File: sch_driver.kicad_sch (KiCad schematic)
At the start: 31 parts, among them Q1 PSMN4R0-30YLDX, Q2 PSMN4R0-30YLDX, Q3 PSMN4R0-30YLDX, Q4 PSMN4R0-30YLDX, U1 ADA4099-2xR, U10 TMUX1112PWR, U2 ADA4099-2xR

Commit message: WIP - Updating analog switch
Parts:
- removed U10: TMUX1112PWR, $Local:TSSOP-16_4.4x5mm_P0.65mm, symbol $Local:TMUX1112PWR
- added U11, U12, U13, U14, U3: TS5A3159ADCK, $Local:SOT-363_SC-70-6, symbol $Local:TS5A3159ADCK
- renumbered C10 to C3, C9 to C4
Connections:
- net DAC1: now also U11.1, U13.1
- net DAC2: now also U12.1, U14.1
- net GND: now also U11.3, U12.3, U13.3, U14.3
- net REF1: now also U11.4; no longer R21.1
- net REF2: now also U12.4; no longer R22.1
- net REF3: now also U13.4; no longer R23.1
- net REF4: now also U14.4; no longer R24.1
- net SEL1: now also R21.1, U11.6
- net SEL2: now also U12.6
- net SEL3: now also U13.6
- net SEL4: now also U14.6
- no-connect marks 2 -> 0
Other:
- moved on the sheet: C11, C13, C3, C4, Q1, Q3, R1, R11, R13, R21, R23, R3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

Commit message: New analog switch drawn. Updated page borders to B-size sheets.
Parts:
- removed C3, C4: 100nF 50V, $Local:C_0603_1608Metric, symbol $Local:C_0603_100NF_50V
- added C11, C12, C13, C14: 100nF 50V, $Local:C_0603_1608Metric, symbol $Local:C_0603_100NF_50V
- added unit 2 of U12
- added unit 2 of U13
- added unit 2 of U14
- renumbered U3 to U11
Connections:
- net +3.3V: now also U11.5 (V+), C11.1, C12.1, C13.1, C14.1, U12.5 (V+), U13.5 (V+), U14.5 (V+)
- net GND: now also U11.2 (GND), C11.2, C12.2, C13.2, C14.2, U12.2 (GND), U13.2 (GND), U14.2 (GND)
- net SEL2: now also R22.1
- net SEL3: now also R23.1
- net SEL4: now also R24.1
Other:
- moved on the sheet: C1, C11, C12, C13, C14, C2, Q1, Q2, Q3, Q4, R1, R11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

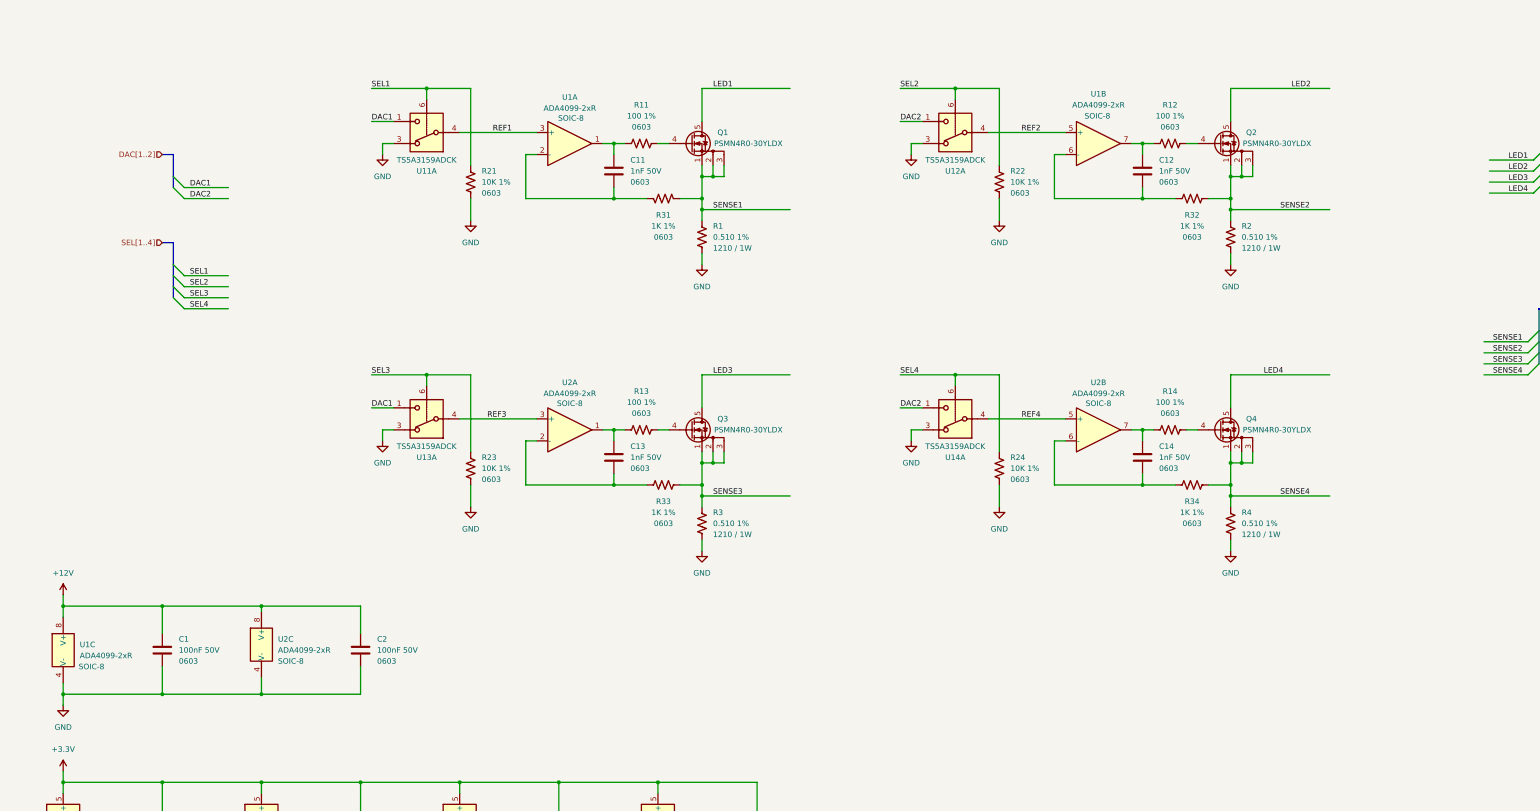
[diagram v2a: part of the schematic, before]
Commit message: Added buffers to current sense signals
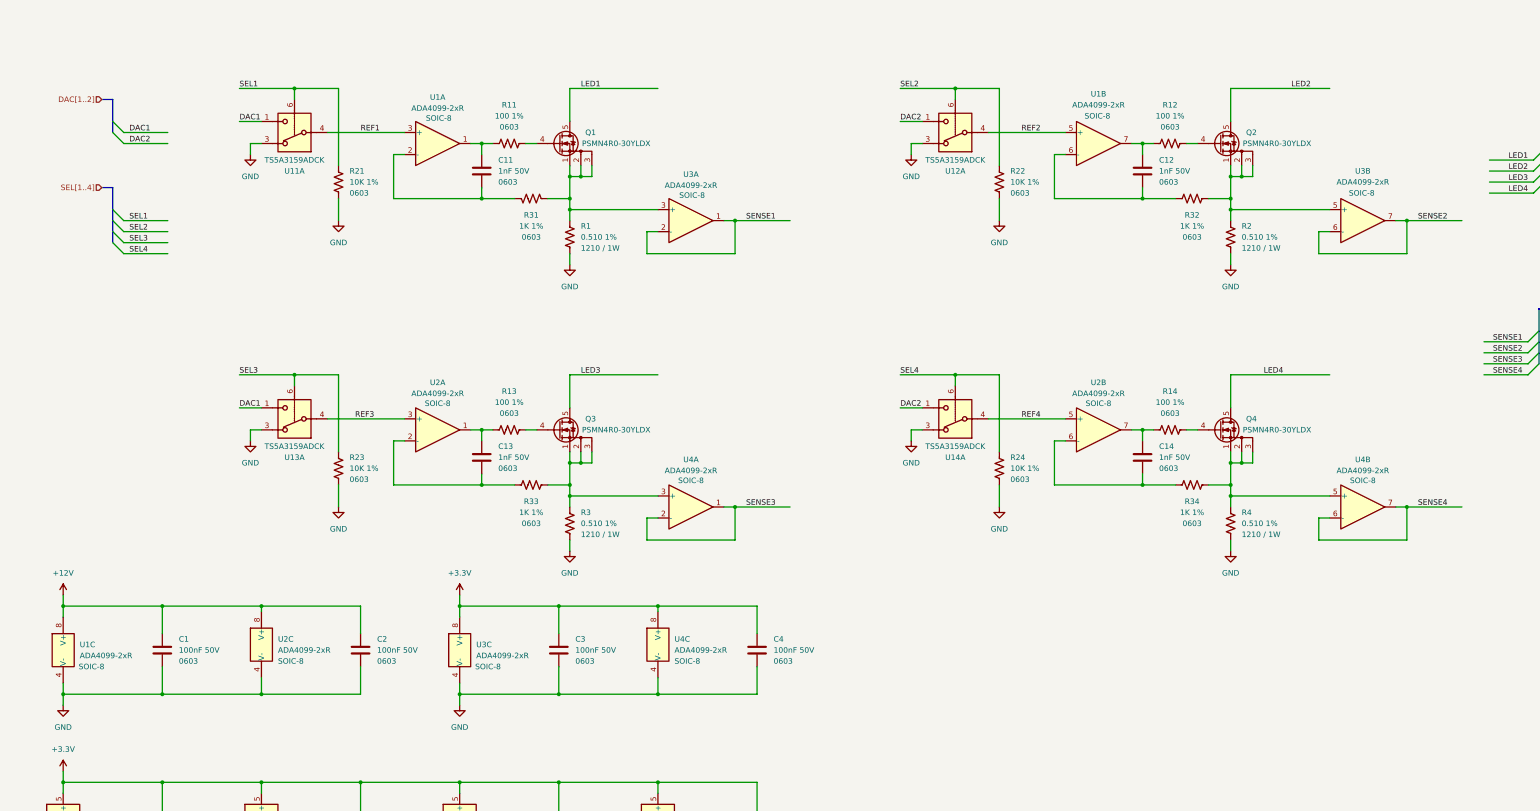
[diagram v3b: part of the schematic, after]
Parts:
- added C3, C4: 100nF 50V, $Local:C_0603_1608Metric, symbol $Local:C_0603_100NF_50V
- added U3, U4: ADA4099-2xR, $Local:SOIC-8_3.9x4.9mm_P1.27mm, symbol $Local:ADA4099-2xR
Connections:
- net +3.3V: now also C3.1, C4.1, U3.8 (V+), U4.8 (V+)
- net GND: now also C3.2, C4.2, U3.4 (V-), U4.4 (V-)
- net SENSE1: now also U3.1, U3.2 (-); no longer Q1.1 (S), Q1.2 (S), Q1.3 (S), R1.1, R31.2
- net SENSE2: now also U3.6 (-), U3.7; no longer Q2.1 (S), Q2.2 (S), Q2.3 (S), R2.1, R32.2
- net SENSE3: now also U4.1, U4.2 (-); no longer Q3.1 (S), Q3.2 (S), Q3.3 (S), R3.1, R33.2
- net SENSE4: now also U4.6 (-), U4.7; no longer Q4.1 (S), Q4.2 (S), Q4.3 (S), R34.2, R4.1
- new net: Q4.1 (S), Q4.2 (S), Q4.3 (S), R34.2, R4.1, U4.5 (+)
- new net: Q3.1 (S), Q3.2 (S), Q3.3 (S), R3.1, R33.2, U4.3 (+)
- new net: Q2.1 (S), Q2.2 (S), Q2.3 (S), R2.1, R32.2, U3.5 (+)
- new net: Q1.1 (S), Q1.2 (S), Q1.3 (S), R1.1, R31.2, U3.3 (+)
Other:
- moved on the sheet: C11, C13, Q1, Q3, R1, R11, R13, R21, R23, R3, R31, R33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

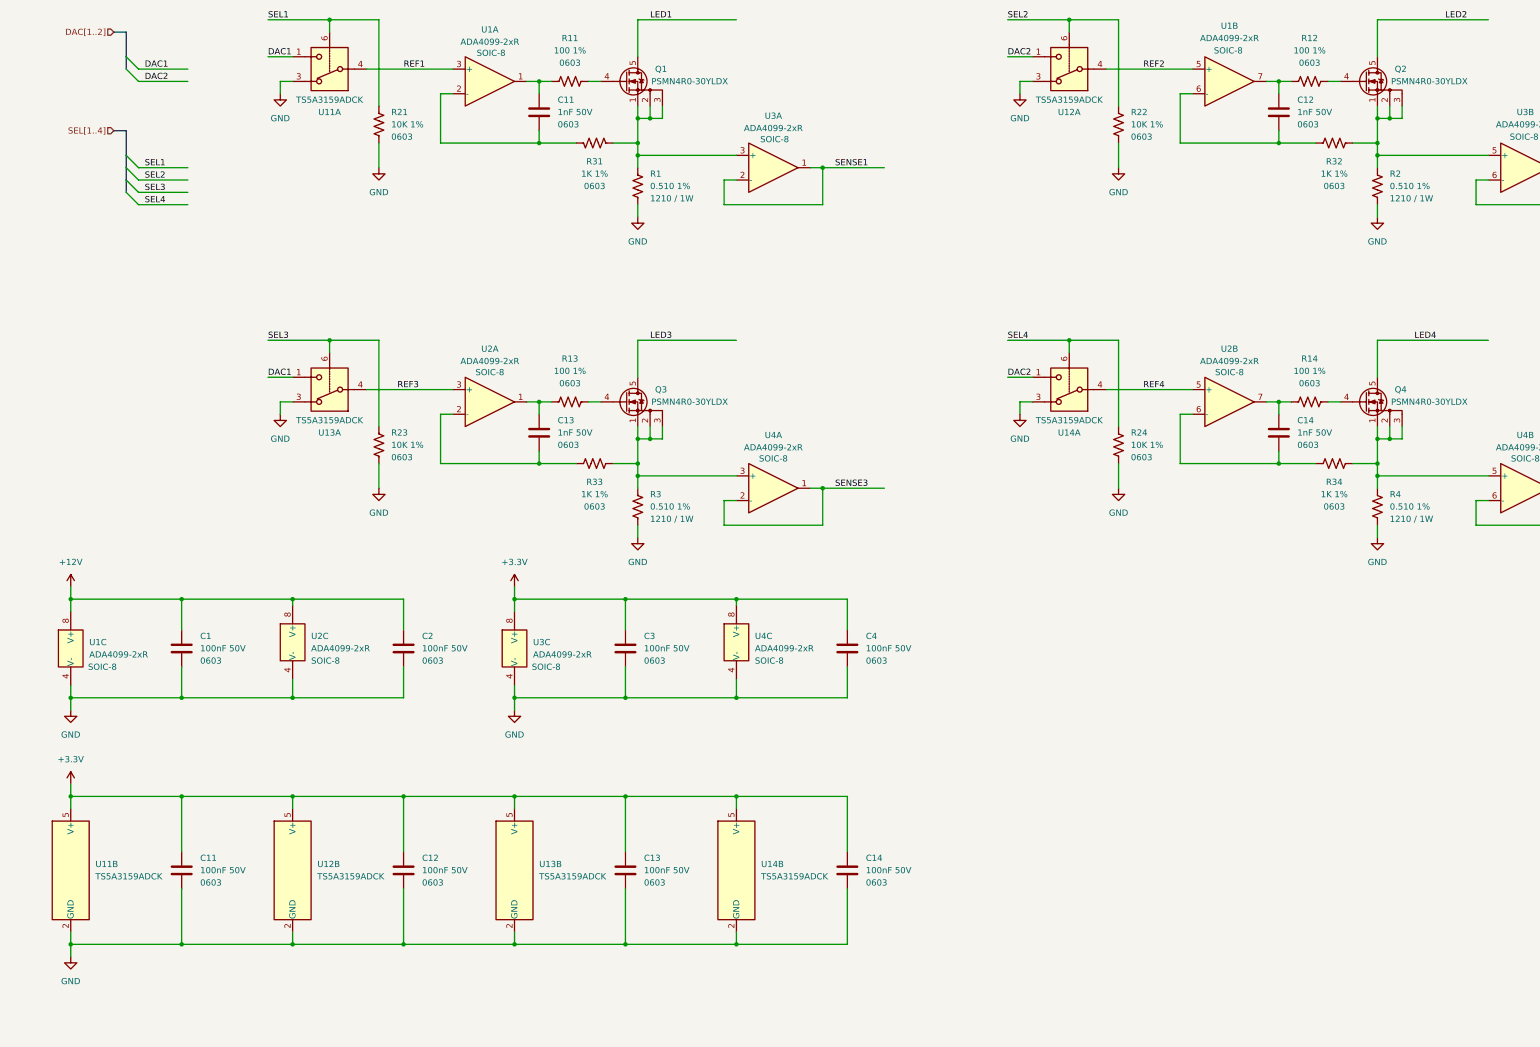
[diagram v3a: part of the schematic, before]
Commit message: Updated 'Size' property to 'Package' on R & C. Cleaned up switch page.
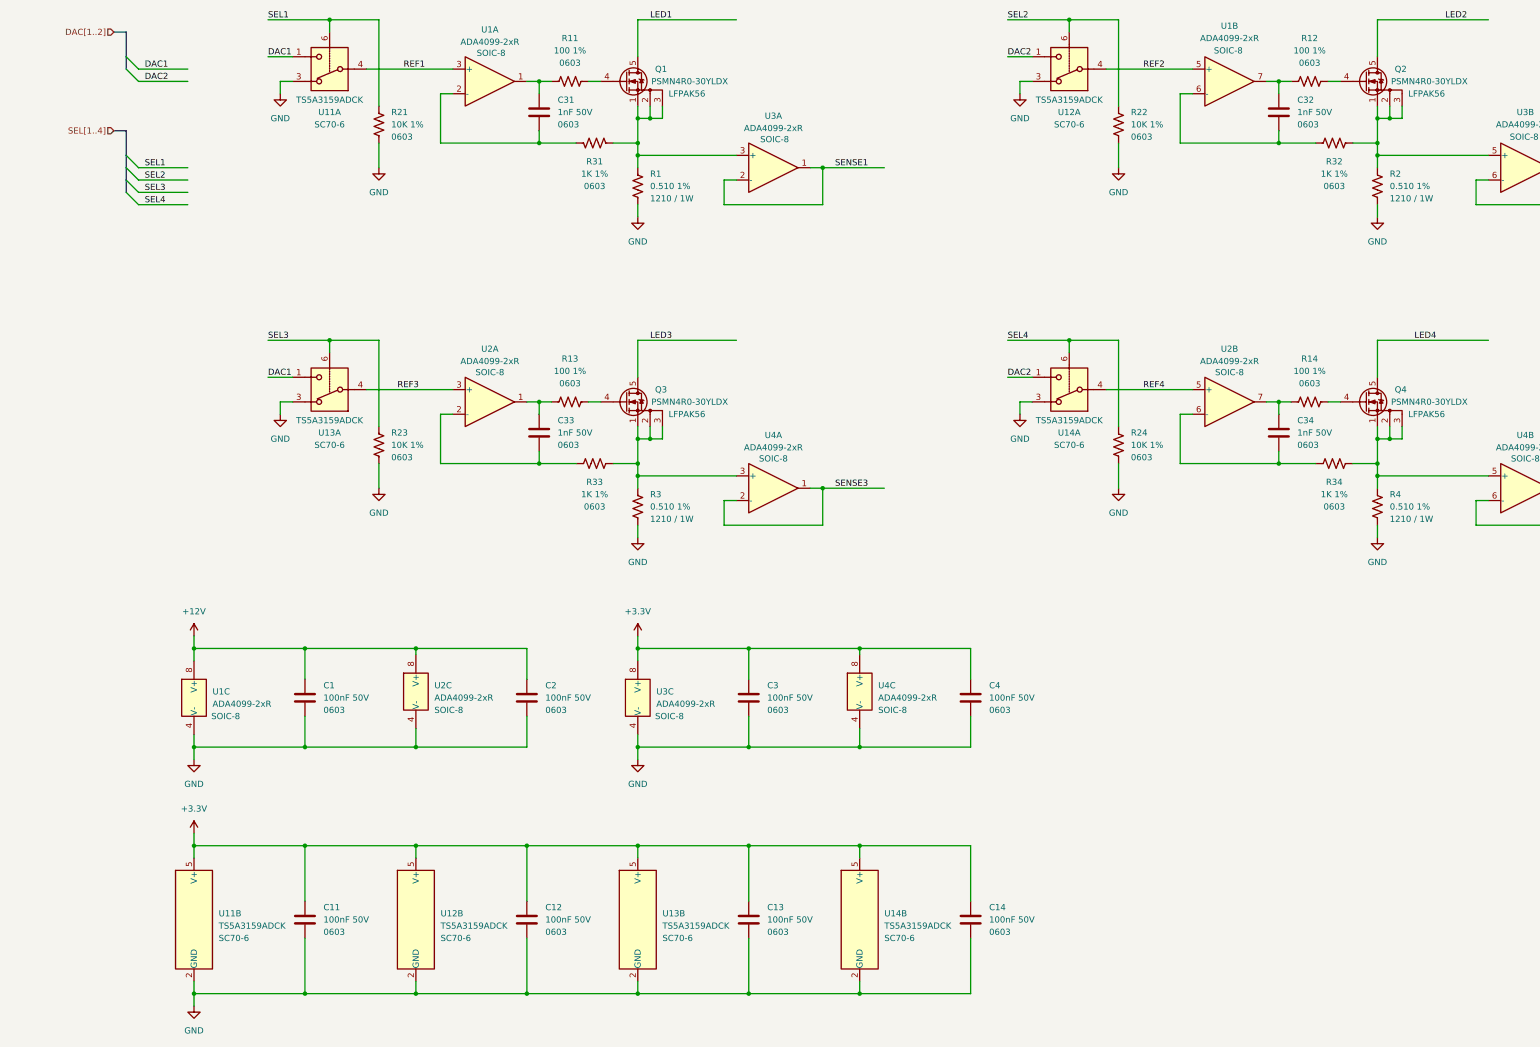
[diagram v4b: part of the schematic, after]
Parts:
- C1, C11, C12, C13, C14, C2, C3, C4, R11, R12, R13, R14, R21, R22, R23, R24, R31, R32, R33, R34: Package (none) -> 0603; Size 0603 -> (none)
- C31: renamed from C11; Package (none) -> 0603; Size 0603 -> (none)
- C32: renamed from C12; Package (none) -> 0603; Size 0603 -> (none)
- C33: renamed from C13; Package (none) -> 0603; Size 0603 -> (none)
- C34: renamed from C14; Package (none) -> 0603; Size 0603 -> (none)
- Q1, Q2, Q3, Q4: Package (none) -> LFPAK56
- R1, R2, R3, R4: Package (none) -> 1210 / 1W; Size 1210 / 1W -> (none)
- U11, U12, U13, U14: Package (none) -> SC70-6
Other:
- moved on the sheet: C1, C11, C12, C13, C14, C2, C3, C4, U11B, U12B, U13B, U14B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

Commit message: Added active LP filter to sense signals. First pass of part placement on 30x70 mm PCB.
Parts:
- removed C3, C4: 100nF 50V, $Local:C_0603_1608Metric, symbol $Local:C_0603_100NF_50V
- removed U3, U4: ADA4099-2xR, $Local:SOIC-8_3.9x4.9mm_P1.27mm, symbol $Local:ADA4099-2xR
- added C21, C22, C23, C24, C61, C62, C63, C64: 100nF 50V, $Local:C_0603_1608Metric, symbol $Local:C_0603_100NF_50V
- added C41, C42, C43, C44: 1uF 50V, $Local:C_0603_1608Metric, symbol $Local:C_0603_1NF_50V
- added R41, R42, R43, R44, R51, R52, R53, R54: 10K 1%, $Local:R_0603_1608Metric, symbol $Local:R_0603_10K
- added R61, R62, R63, R64: 90.9K 1%, $Local:R_0603_1608Metric, symbol $Local:R_0603_10K
- added U21, U22, U23, U24: OPA333, Package_TO_SOT_SMD:SOT-353_SC-70-5, symbol $Local:OPA333
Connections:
- net +3.3V: now also C21.1, C22.1, C23.1, C24.1, U21.5 (V+), U22.5 (V+), U23.5 (V+), U24.5 (V+)
- net GND: now also C21.2, C22.2, C23.2, C24.2, C41.2, C42.2, C43.2, C44.2, R51.2, R52.2, R53.2, R54.2, U21.2 (V-), U22.2 (V-), U23.2 (V-), U24.2 (V-)
- net SENSE1: now also C61.1, R61.1, U21.4
- net SENSE2: now also C62.1, R62.1, U22.4
- net SENSE3: now also C63.1, R63.1, U23.4
- net SENSE4: now also C64.1, R64.1, U24.4
- net at Q4.1 (S), Q4.2 (S), Q4.3 (S)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: now also R44.2
- net at Q3.1 (S), Q3.2 (S), Q3.3 (S)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: now also R43.2
- net at Q2.1 (S), Q2.2 (S), Q2.3 (S)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: now also R42.2
- net at Q1.1 (S), Q1.2 (S), Q1.3 (S)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: now also R41.2
- new net: C61.2, R51.1, R61.2, U21.3 (-)
- new net: C62.2, R52.1, R62.2, U22.3 (-)
- new net: C64.2, R54.1, R64.2, U24.3 (-)
- new net: C42.1, R42.1, U22.1 (+)
- new net: C63.2, R53.1, R63.2, U23.3 (-)
- new net: C44.1, R44.1, U24.1 (+)
- new net: C43.1, R43.1, U23.1 (+)
- new net: C41.1, R41.1, U21.1 (+)
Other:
- moved on the sheet: C1, C11, C12, C13, C14, C2, C31, C32, C33, Q1, Q2, Q3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
